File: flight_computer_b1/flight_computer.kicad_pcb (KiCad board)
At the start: 4 copper layers, 78 x 67 mm, 107 parts, among them J1 Pi Connector, J2 Conn_02x02_Odd_Even, J3 Conn_01x03, J4 DB25_Socket, J5 DB25_Socket, Q1 MMBT3904, U1 IRLML6344TRPBF, U10 CD74HC4067SM, U11 IRLML6344TRPBF, U12 LM66200DRLR, U2 IRLML6344TRPBF, U3 IRLML6344TRPBF, U4 IRLML6344TRPBF, U5 LMR51430XDDCR, U6 ADS1158IRTCR, U8 MCP6001-OT, U9 MCP6001-OT, Y1 32.768kHz

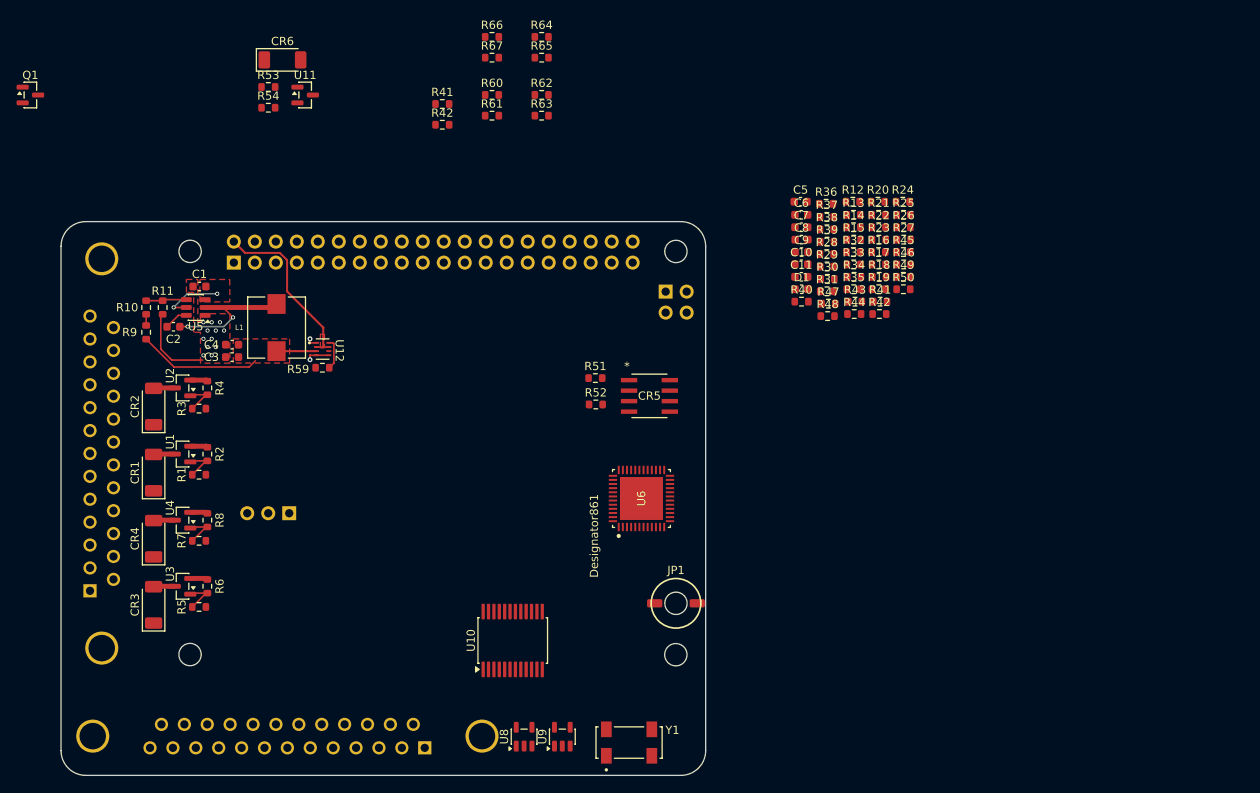
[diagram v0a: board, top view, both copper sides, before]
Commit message: flight computer: routing updates
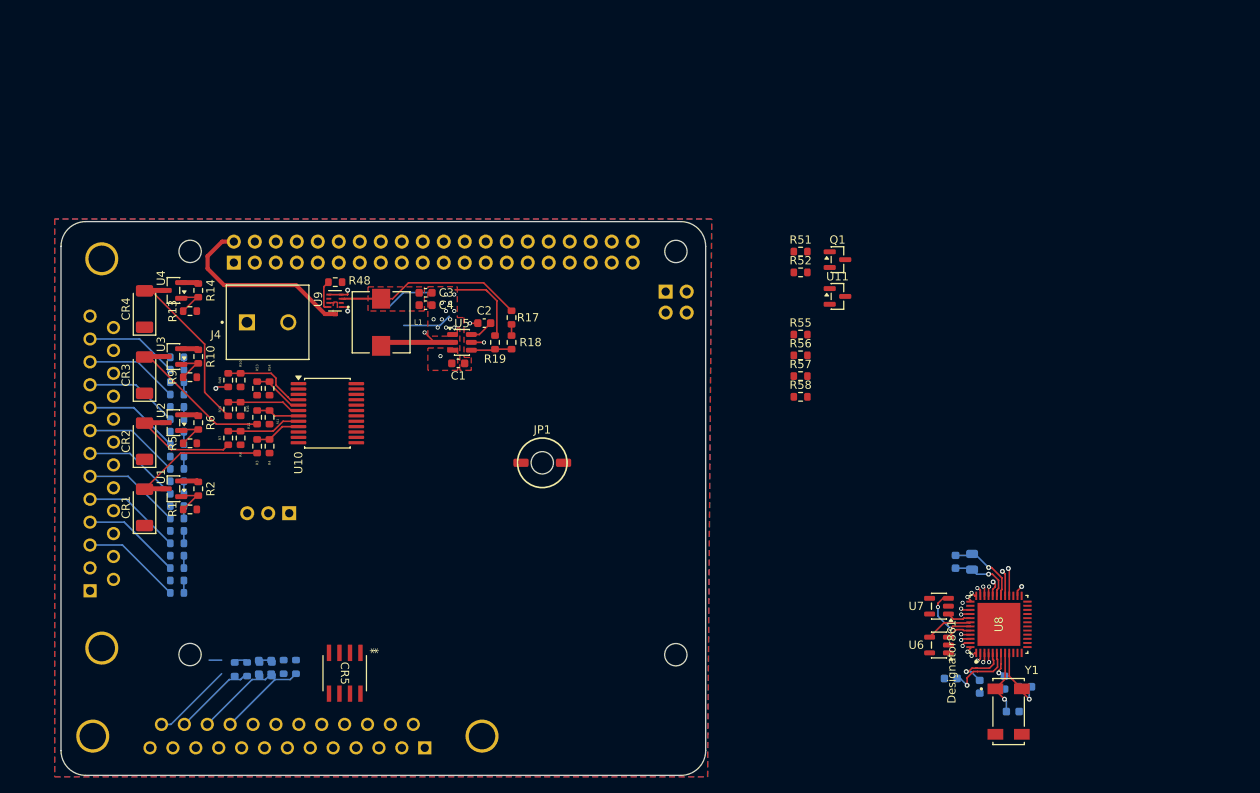
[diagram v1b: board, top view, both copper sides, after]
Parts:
- removed the C5 at (192.0, 68.9)
- removed CR6: STPS360AF, Diode_SMD:D_SOD-128
- removed D1: LED, Capacitor_SMD:C_0603_1608Metric
- removed the R40 at (192.1, 81.0)
- removed the R41 at (148.6, 57.1)
- removed the R41 at (201.6, 81.0)
- removed the R42 at (148.6, 59.6)
- removed the R42 at (201.5, 82.5)
- removed the R43 at (198.6, 81.0)
- removed the R44 at (198.5, 82.5)
- removed the R45 at (204.4, 75.0)
- removed the R46 at (204.4, 76.5)
- removed the R47 at (195.3, 81.3)
- removed the R48 at (195.2, 82.8)
- removed the R49 at (204.4, 78.0)
- removed the R50 at (204.4, 79.5)
- removed R62, R64, R66: 4k, Resistor_SMD:R_0603_1608Metric
- removed R63, R65, R67: 1k, Resistor_SMD:R_0603_1608Metric
- removed the U6 at (172.7, 104.8)
- added C11: 10uF, Capacitor_SMD:C_0603_1608Metric, B.Cu at (213.6, 127.6)
- added J4: Screw_Terminal_01x02, avi_lib:PHOENIX_1935776, F.Cu at (122.5, 88.0)
- added R11: 4k, Resistor_SMD:R_0603_1608Metric, F.Cu at (126.2, 95.0)
- added R12: 1k, Resistor_SMD:R_0603_1608Metric, F.Cu at (127.7, 95.0)
- added R15: 4k, Resistor_SMD:R_0603_1608Metric, F.Cu at (122.7, 94.0)
- added R16: 1k, Resistor_SMD:R_0603_1608Metric, F.Cu at (124.2, 94.0)
- added R51: 100, Resistor_SMD:R_0603_1608Metric, F.Cu at (192.0, 75.0)
- added R52: 1k, Resistor_SMD:R_0603_1608Metric, F.Cu at (192.0, 77.5)
- added R55: 4k, Resistor_SMD:R_0603_1608Metric, F.Cu at (192.0, 85.0)
- added R56: 10k, Resistor_SMD:R_0603_1608Metric, F.Cu at (192.0, 87.5)
- added R57: 1k, Resistor_SMD:R_0603_1608Metric, F.Cu at (192.0, 90.0)
- added R58: 1k, Resistor_SMD:R_0603_1608Metric, F.Cu at (192.0, 92.5)
- added R7: 4k, Resistor_SMD:R_0603_1608Metric, F.Cu at (122.7, 97.5)
- added R8: 1k, Resistor_SMD:R_0603_1608Metric, F.Cu at (124.2, 97.5)
- added U8: ADS1158IRTCR, avi_lib:RTC0048A-IPC_A, F.Cu at (216.0, 120.1)
- C10: renamed from C11; moved to B.Cu
- C5: renamed from C7; footprint Capacitor_SMD:C_0603_1608Metric -> Capacitor_SMD:C_0805_2012Metric; moved to B.Cu
- C6: moved to B.Cu
- C7: renamed from C8; moved to B.Cu
- C8: renamed from C9; moved to B.Cu
- C9: renamed from C10; moved to B.Cu
- L1: value CLF7045NIT-6R8N-D -> 6.8uH
- R20: renamed from R12; moved to B.Cu
- R21: renamed from R13; moved to B.Cu
- R22: renamed from R14; moved to B.Cu
- R23: renamed from R15; moved to B.Cu
- R24: renamed from R16; moved to B.Cu
- R25: renamed from R17; moved to B.Cu
- R26: renamed from R18; moved to B.Cu
- R27: renamed from R19; moved to B.Cu
- R28: renamed from R20; moved to B.Cu
- R29: renamed from R21; moved to B.Cu
- R30: renamed from R22; moved to B.Cu
- R31: renamed from R23; moved to B.Cu
- R32: renamed from R24; moved to B.Cu
- R33: renamed from R25; moved to B.Cu
- R34: renamed from R26; moved to B.Cu
- R35: renamed from R27; moved to B.Cu
- R36: renamed from R28; moved to B.Cu
- R37: renamed from R29; moved to B.Cu
- R38: renamed from R30; moved to B.Cu
- R39: renamed from R31; moved to B.Cu
- R40: renamed from R32; moved to B.Cu
- R41: renamed from R33; moved to B.Cu
- R42: renamed from R34; moved to B.Cu
- R43: renamed from R35; moved to B.Cu
- R44: renamed from R36; moved to B.Cu
- R45: renamed from R37; moved to B.Cu
- R46: renamed from R38; moved to B.Cu
- R47: renamed from R39; moved to B.Cu
- R53: value 100 -> 4k
- U5: value LMR51430XDDCR -> LMR51430XFDDCR
- moved Q1 99.7 mm to (196.4, 75.9)
- moved R24 94.4 mm to (116.5, 116.2)
- moved R25 93.1 mm to (116.5, 114.8), turned to 180 degrees
- moved R32 92.6 mm to (116.5, 98.2)
- moved R26 92.0 mm to (116.5, 113.2)
- moved R28 91.9 mm to (116.5, 104.2)
- moved R33 91.7 mm to (116.5, 96.8), turned to 180 degrees
- moved R20 91.6 mm to (116.5, 110.2)
- moved R34 90.9 mm to (116.5, 95.2)
- moved R27 90.8 mm to (116.5, 111.8), turned to 180 degrees
- moved R29 90.8 mm to (116.5, 102.8), turned to 180 degrees
- moved R21 90.3 mm to (116.5, 108.8), turned to 180 degrees
- moved R35 90.2 mm to (116.5, 93.8), turned to 180 degrees
- moved R30 89.8 mm to (116.5, 101.2)
- moved R22 89.1 mm to (116.5, 107.2)
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- renumbered H3 to H2, H2 to H3, J5 to J1, J4 to J2, J1 to J5, J2 to J6, R6 to R10, R7 to R13, R8 to R14, R9 to R17, R10 to R18, R11 to R19, R60 to R3, R61 to R4, R59 to R48, R51 to R49, R3 to R5, R52 to R50, R4 to R6, R5 to R9, U8 to U6, U9 to U7, U12 to U9
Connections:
- C5 pad 1: +5V -> /adc0/VREFP
- C5 pad 2: GND -> /adc0/VREFN
- C7 pad 1: +5V -> /adc0/VREFP
- C7 pad 2: GND -> /adc0/VREFN
- CR5 pad 5: /rs485/RS485_TX+ -> /ESC_RX+
- CR5 pad 6: /rs485/RS485_TX- -> /ESC_RX-
- CR5 pad 7: /rs485/RS485_RX- -> /ESC_TX-
- CR5 pad 8: /rs485/RS485_RX+ -> /ESC_TX+
- J1 pad 10: unconnected-(J5-Pad10) -> /ESC_RX-
- J1 pad 11: unconnected-(J5-Pad11) -> /ESC_TX+
- J1 pad 12: unconnected-(J5-Pad12) -> /ESC_TX-
- J1 pad 20: unconnected-(J5-P20-Pad20) -> +24V
- J1 pad 21: unconnected-(J5-P21-Pad21) -> /PT_GND
- J1 pad 22: unconnected-(J5-P22-Pad22) -> /PT_5+
- J1 pad 23: unconnected-(J5-P23-Pad23) -> /PT_5-
- J1 pad 24: unconnected-(J5-P24-Pad24) -> /PT_6+
- J1 pad 25: unconnected-(J5-P25-Pad25) -> /PT_6-
- J1 pad 9: unconnected-(J5-Pad9) -> /ESC_RX+
- J2 pad 1: unconnected-(J4-Pad1) -> +24V
- J2 pad 10: /PT_2- -> /PT_3-
- J2 pad 11: /PT_3+ -> /PT_4+
- J2 pad 12: /PT_3- -> /PT_4-
- J2 pad 13: /PT_4+ -> unconnected-(J2-Pad13)
- J2 pad 14: /PT_4- -> unconnected-(J2-P14-Pad14)
- J2 pad 2: unconnected-(J4-Pad2) -> /PT_GND
- J2 pad 21: unconnected-(J4-P21-Pad21) -> +24V
- J2 pad 22: unconnected-(J4-P22-Pad22) -> /valve2_excitation_return
- J2 pad 23: unconnected-(J4-P23-Pad23) -> +24V
- J2 pad 24: unconnected-(J4-P24-Pad24) -> /valve3_excitation_return
- J2 pad 5: unconnected-(J4-Pad5) -> /PT_1+
- J2 pad 6: unconnected-(J4-Pad6) -> /PT_1-
- J2 pad 7: /PT_1+ -> /PT_2+
- J2 pad 8: /PT_1- -> /PT_2-
- J2 pad 9: /PT_2+ -> /PT_3+
- R53 pad 1: /PYRO_FIRE -> /pyro_excitation_return
- R53 pad 2: Net-(U11-G) -> /mux_input4
- R54 pad 1: Net-(U11-G) -> /mux_input4
- U1 pad 1: /valve0_excitation_return -> Net-(U1-G)
- U1 pad 2: Net-(U1-G) -> GND
- U1 pad 3: GND -> /valve0_excitation_return
- U10 pad 15: /mux0/~{enable} -> GND
- U2 pad 1: /valve1_excitation_return -> Net-(U2-G)
- U2 pad 2: Net-(U2-G) -> GND
- U2 pad 3: GND -> /valve1_excitation_return
- U3 pad 1: /valve2_excitation_return -> Net-(U3-G)
- U3 pad 2: Net-(U3-G) -> GND
- U3 pad 3: GND -> /valve2_excitation_return
- U4 pad 1: /valve3_excitation_return -> Net-(U4-G)
- U4 pad 2: Net-(U4-G) -> GND
- U4 pad 3: GND -> /valve3_excitation_return
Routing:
- net GND: track 22.4 -> 40.6 mm, vias 14 -> 17
- net +5V: track 21.2 -> 38.4 mm, vias 0 -> 4
- net /valve0_excitation_return: track 2.58 -> 18.0 mm
- net /valve3_excitation_return: track 7.22 -> 22.4 mm
- net /PT_2+: track 0.00 -> 12.4 mm
- net /valve2_excitation_return: track 7.22 -> 19.6 mm
- net /PT_0+: track 0.00 -> 12.1 mm
- net /PT_0-: track 0.00 -> 12.0 mm
- net /PT_1+: track 0.00 -> 11.9 mm
- net /PT_1-: track 0.00 -> 11.8 mm
- net /PT_2-: track 0.00 -> 11.6 mm
- net /PT_3+: track 0.00 -> 11.5 mm
- net /PT_3-: track 0.00 -> 11.4 mm
- net /PT_4+: track 0.00 -> 11.3 mm
- net /PT_4-: track 0.00 -> 11.2 mm
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- added copper zone on In1.Cu, net +24V
- added copper zone on B.Cu, net GND

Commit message: flight computer: new pyro circuit
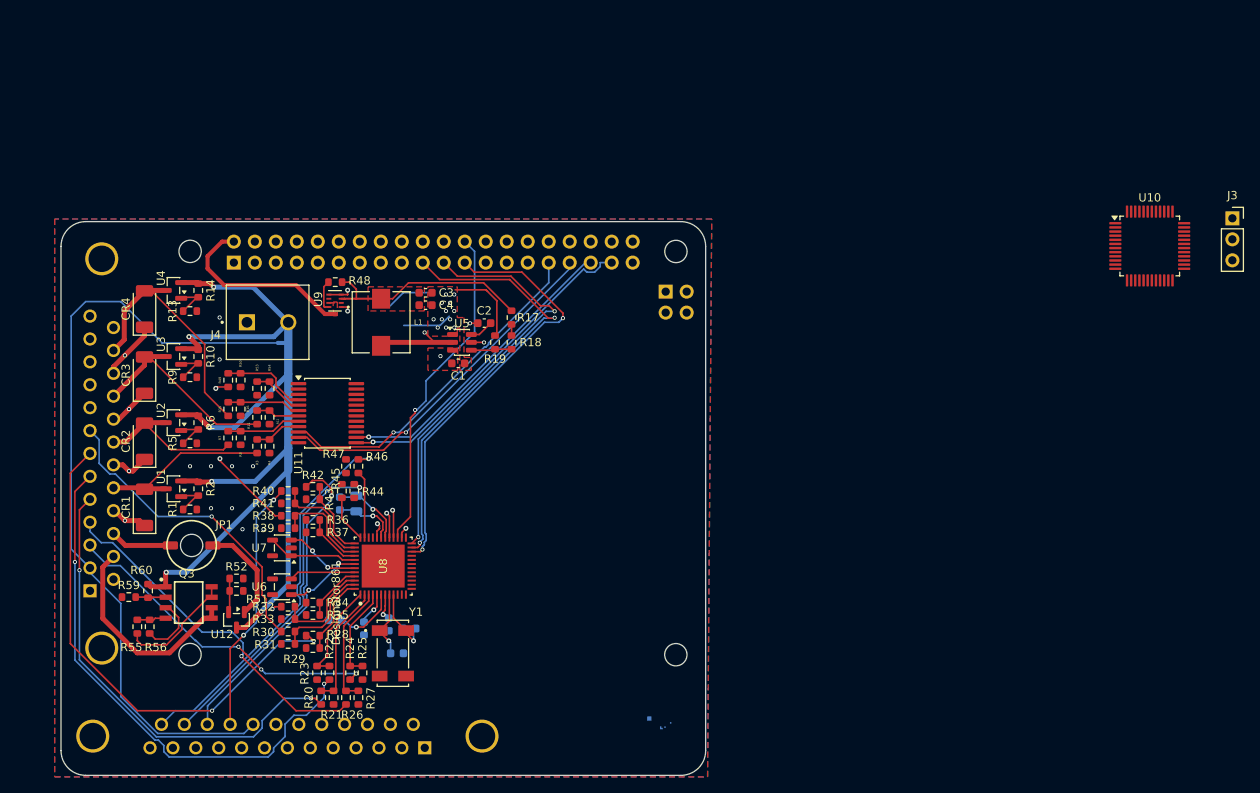
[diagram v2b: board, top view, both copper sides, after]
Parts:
- removed CR5: ST490ABDR, avi_lib:SO-8_STM
- removed Q1: MMBT3904, Package_TO_SOT_SMD:SOT-23
- removed R57, R58: 1k, Resistor_SMD:R_0603_1608Metric
- added G***: LOGO, avi_lib:qr-code, B.Cu at (175.2, 133.0)
- added NT1: NetTie_2, NetTie:NetTie-2_SMD_Pad0.5mm, B.Cu at (129.2, 86.0)
- added Q3: ISA170230C04LMDS, avi_lib:PG-DSO-8-920-V, F.Cu at (117.9, 117.4)
- added R59: 100, Resistor_SMD:R_0603_1608Metric, F.Cu at (110.7, 116.8)
- added R60: 1k, Resistor_SMD:R_0603_1608Metric, F.Cu at (113.0, 116.0)
- added U10: LTC2983, Package_QFP:LQFP-48_7x7mm_P0.5mm, F.Cu at (234.2, 74.3)
- J3, R20, R21, R22, R23, R24, R25, R26, R27, R28, R29, R30, R31, R32, R33, R34, R35, R36, R37, R38, R39, R40, R41, R42, R43, R44, R45, R46, R47: moved to F.Cu
- R55: value 4k -> 2k
- R56: value 10k -> 1k
- moved J3 119.6 mm to (244.2, 70.9), turned to 0 degrees
- moved R55 87.7 mm to (111.7, 120.3), turned to 90 degrees
- moved R56 85.3 mm to (113.2, 120.3), turned to -90 degrees
- moved U12 82.6 mm to (123.7, 119.5), turned to -90 degrees
- moved U6 79.8 mm to (129.2, 115.5)
- moved U7 79.8 mm to (129.2, 110.8)
- moved R51 79.6 mm to (123.7, 116.0), turned to 180 degrees
- moved R52 77.7 mm to (123.7, 114.5)
- moved C10 74.8 mm to (144.6, 120.6)
- moved C11 74.8 mm to (139.1, 120.6)
- moved C5 74.8 mm to (138.2, 105.4)
- moved C6 74.8 mm to (135.6, 119.6)
- moved C7 74.8 mm to (136.2, 105.4)
- moved C8 74.8 mm to (142.1, 120.1)
- moved C9 74.8 mm to (143.1, 123.6)
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- renumbered U10 to U11, U11 to U12
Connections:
- net Net-(Q1-B) renamed /pyro0/POWER_ENABLE
- J5 pad 10: /RS485_UART_RX -> /UART_ESC_RX
- J5 pad 8: /RS485_UART_TX -> /UART_ESC_TX
- R55 pad 1: /PYRO_ARM -> Net-(Q3-Pad7)
- R56 pad 2: GND -> +24V
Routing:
- net GND: track 40.6 -> 155.9 mm, vias 17 -> 33
- net /PT_GND: track 0.00 -> 94.6 mm
- net /ADC_DIN: track 0.00 -> 55.2 mm, vias 0 -> 2
- net /PT_1-: track 11.8 -> 65.1 mm, vias 0 -> 2
- net /ADC_SCLK: track 0.00 -> 52.6 mm, vias 0 -> 2
- net /ADC_DOUT: track 0.00 -> 51.7 mm, vias 0 -> 2
- net /PT_2+: track 12.4 -> 62.1 mm, vias 0 -> 2
- net /PT_1+: track 11.9 -> 55.8 mm, vias 0 -> 2
- net /mux_addr1: track 0.00 -> 43.3 mm, vias 0 -> 1
- net /mux_addr0: track 0.00 -> 41.8 mm, vias 0 -> 1
- net /mux_addr3: track 0.00 -> 40.7 mm, vias 0 -> 1
- net /ADC_CS: track 0.00 -> 40.3 mm, vias 0 -> 1
- net /mux_addr2: track 0.00 -> 37.1 mm, vias 0 -> 1
- net /PT_6-: track 9.81 -> 46.4 mm, vias 0 -> 1
- net /PT_0-: track 12.0 -> 42.6 mm, vias 0 -> 1
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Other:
- board text added: "Q3"

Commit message: flight computer: almost all routing done
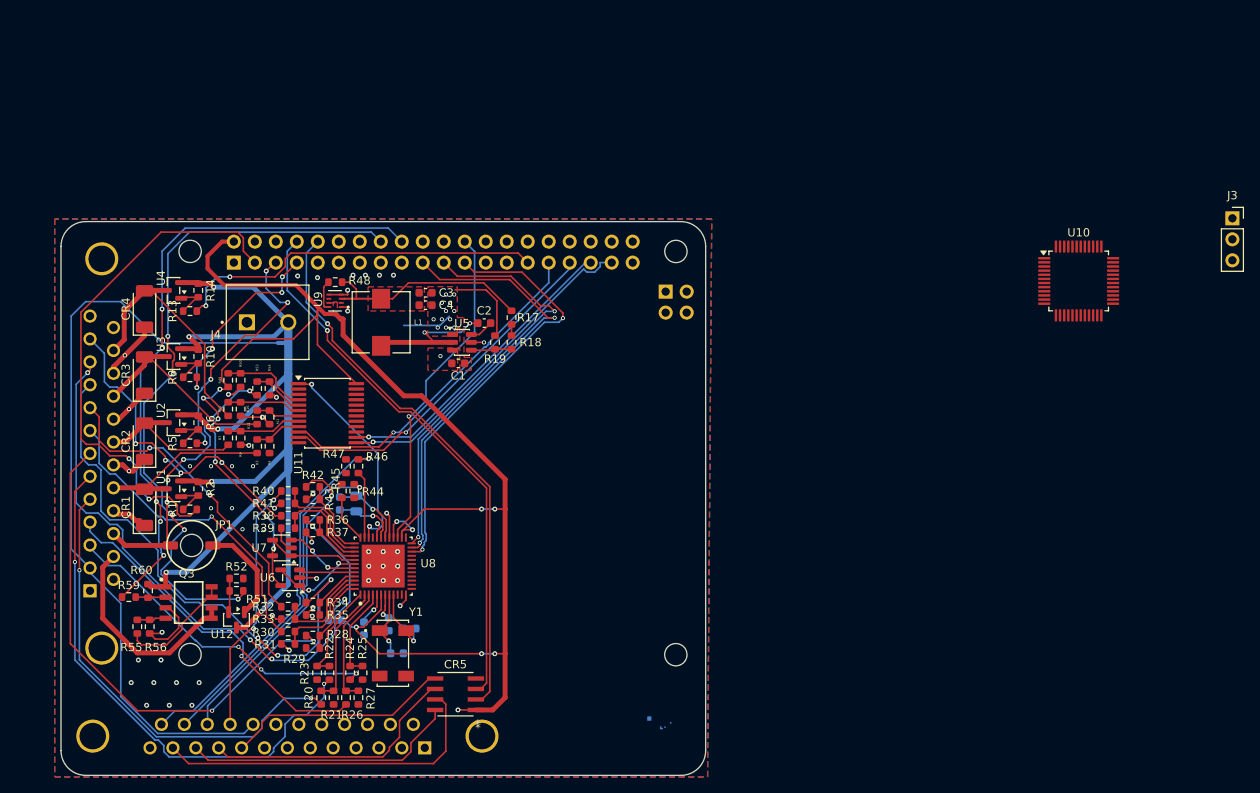
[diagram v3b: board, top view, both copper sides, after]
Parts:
- added CR5: ST490ABDR, avi_lib:SO-8_STM, F.Cu at (150.2, 128.5)
- moved U10 9.58 mm to (225.6, 78.5)
- moved U6 1.49 mm to (130.2, 114.4)
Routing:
- net +5V: track 37.9 -> 193.3 mm, vias 4 -> 14
- net /PYRO_FIRE: track 0.00 -> 83.3 mm, vias 0 -> 5
- net /PYRO_ARM: track 0.00 -> 77.2 mm, vias 0 -> 5
- net /PT_4+: track 0.00 -> 76.3 mm, vias 0 -> 4
- net /UART_ESC_RX: track 0.00 -> 67.2 mm, vias 0 -> 1
- net /UART_ESC_TX: track 0.00 -> 66.3 mm, vias 0 -> 1
- net /PT_3-: track 0.00 -> 65.7 mm, vias 0 -> 3
- net /valve0_enable: track 0.00 -> 63.3 mm, vias 0 -> 2
- net /valve3_enable: track 0.00 -> 45.2 mm, vias 0 -> 2
- net /ESC_TX-: track 0.00 -> 41.6 mm
- net /PT_3+: track 1.19 -> 38.0 mm, vias 1 -> 2
- net /ESC_TX+: track 0.00 -> 33.3 mm
- net /ESC_RX-: track 0.00 -> 31.4 mm
- net /valve1_enable: track 0.00 -> 30.6 mm, vias 0 -> 4
- net /PT_4-: track 10.4 -> 38.8 mm, vias 1 -> 4
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- added copper zone on In2.Cu, net GND

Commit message: tc updates
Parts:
- moved U10 27.7 mm to (200.6, 90.3)
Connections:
- J5 pad 35: /mux_addr2 -> /TEMP_DOUT
- J5 pad 36: unconnected-(J5-Pin_36-Pad36) -> /TEMP_CS
- J5 pad 37: /mux_addr3 -> unconnected-(J5-Pin_37-Pad37)
- J5 pad 38: unconnected-(J5-Pin_38-Pad38) -> /TEMP_DIN
- J5 pad 40: unconnected-(J5-Pin_40-Pad40) -> /TEMP_SCLK
- U10 pad 1: /temperature0/GND -> GND
- U10 pad 11: unconnected-(U10-V_{REF_BYP}-Pad11) -> Net-(U10-V_{REF_BYP})
- U10 pad 12: /temperature0/GND -> GND
- U10 pad 13: unconnected-(U10-V_{REFOUT}-Pad13) -> GND
- U10 pad 14: unconnected-(U10-V_{REFP}-Pad14) -> GND
- U10 pad 15: /temperature0/GND -> GND
- U10 pad 16: unconnected-(U10-CH1-Pad16) -> /TC1+
- U10 pad 17: unconnected-(U10-CH2-Pad17) -> GND
- U10 pad 18: unconnected-(U10-CH3-Pad18) -> /TC2+
- U10 pad 19: unconnected-(U10-CH4-Pad19) -> GND
- U10 pad 2: /temperature0/VDD -> +5V
- U10 pad 20: unconnected-(U10-CH5-Pad20) -> /TC3+
- U10 pad 21: unconnected-(U10-CH6-Pad21) -> GND
- U10 pad 22: unconnected-(U10-CH7-Pad22) -> /TC4+
- U10 pad 23: unconnected-(U10-CH8-Pad23) -> GND
- U10 pad 24: unconnected-(U10-CH9-Pad24) -> /RTD1A
- U10 pad 25: unconnected-(U10-CH10-Pad25) -> /RTD1B
- U10 pad 26: unconnected-(U10-CH11-Pad26) -> /RTD1C
- U10 pad 27: unconnected-(U10-CH12-Pad27) -> /RTD2A
- U10 pad 28: unconnected-(U10-CH13-Pad28) -> /RTD2B
- U10 pad 29: unconnected-(U10-CH14-Pad29) -> /RTD2C
- U10 pad 3: /temperature0/GND -> GND
- U10 pad 36: /temperature0/GND -> GND
- U10 pad 37: unconnected-(U10-INTERRUPT-Pad37) -> /TEMP_INT
- U10 pad 38: /temperature0/SCLK -> /TEMP_SCLK
- U10 pad 39: /temperature0/DOUT -> /TEMP_DOUT
- U10 pad 4: /temperature0/VDD -> +5V
- U10 pad 40: /temperature0/DIN -> /TEMP_DIN
- U10 pad 41: /temperature0/CS -> /TEMP_CS
- U10 pad 42: unconnected-(U10-~{RESET}-Pad42) -> +5V
- U10 pad 43: unconnected-(U10-LDO-Pad43) -> Net-(U10-LDO)
- U10 pad 44: /temperature0/GND -> GND
- U10 pad 45: /temperature0/VDD -> +5V
- U10 pad 46: unconnected-(U10-Q3-Pad46) -> Net-(U10-Q3)
- U10 pad 47: unconnected-(U10-Q2-Pad47) -> Net-(U10-Q2)
- U10 pad 48: unconnected-(U10-Q1-Pad48) -> Net-(U10-Q1)
- U10 pad 5: /temperature0/GND -> GND
- U10 pad 6: /temperature0/VDD -> +5V
- U10 pad 7: /temperature0/GND -> GND
- U10 pad 8: /temperature0/VDD -> +5V
- U10 pad 9: /temperature0/GND -> GND
